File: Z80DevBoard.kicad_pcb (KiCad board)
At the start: 2 copper layers, 143 parts, among them SW1 WAIT, SW2 RESET, SW3 Z80BOOT, SW4 RPBOOT

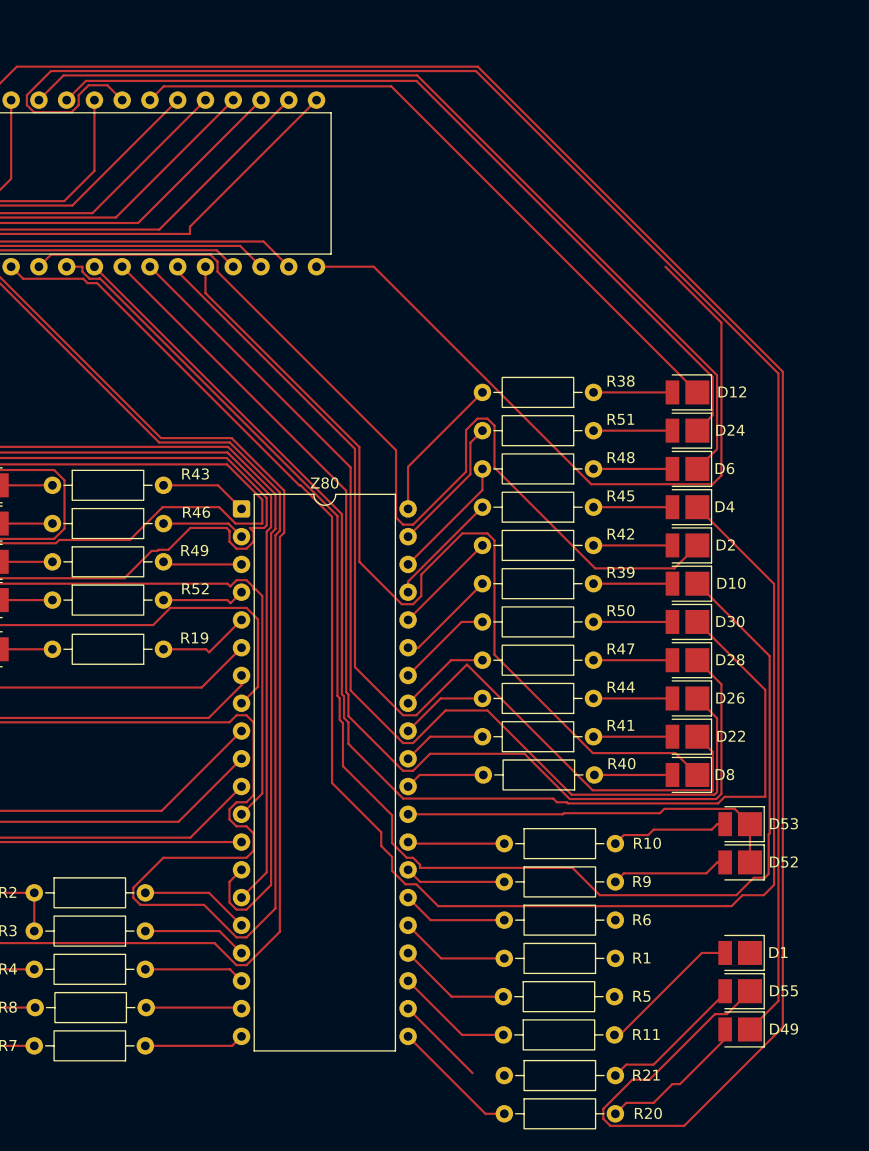
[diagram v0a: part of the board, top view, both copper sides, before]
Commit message: Fixed the GND of the Z80.
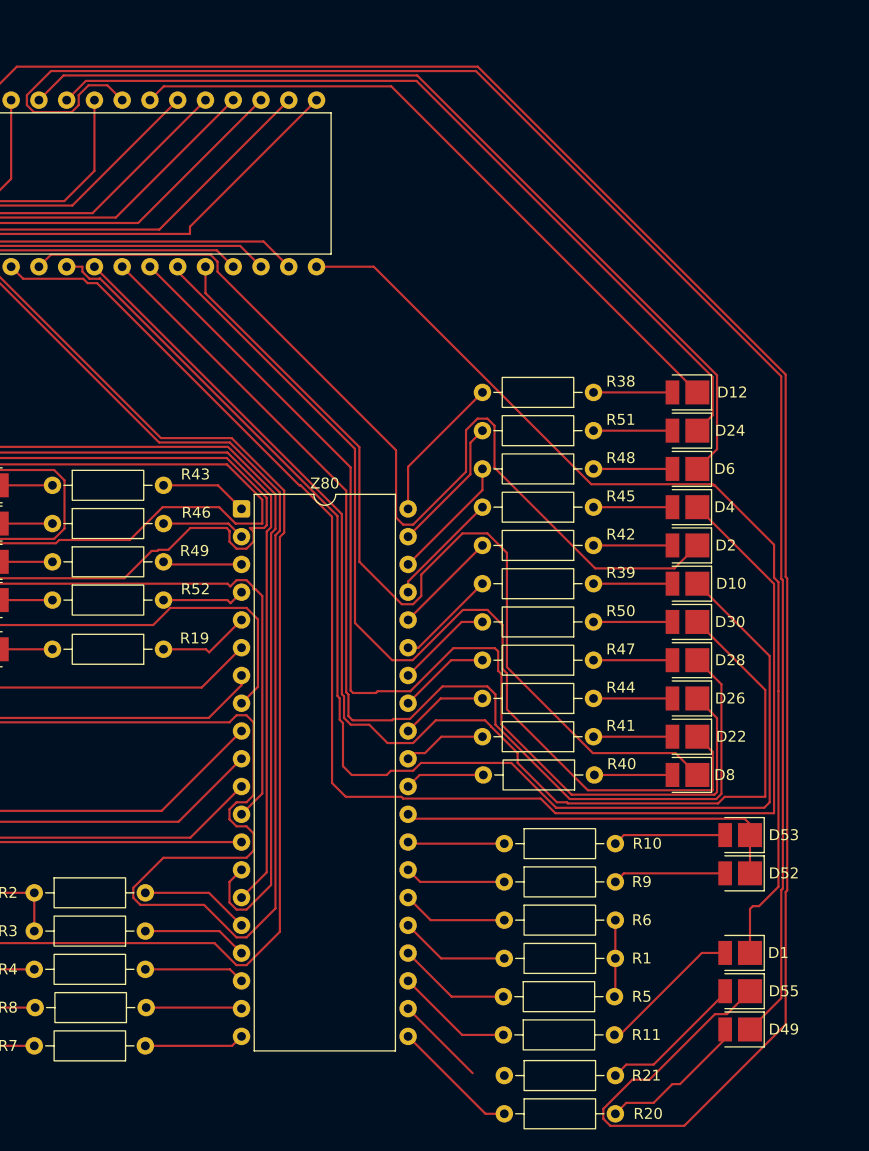
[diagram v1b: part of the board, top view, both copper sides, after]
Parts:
- moved D52 1.00 mm to (151.3, 159.0)
- moved D53 1.00 mm to (151.3, 155.5)
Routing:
- net GND: track 113.9 -> 139.0 mm
- net RAM-A7: track 148.1 -> 135.7 mm
- net RAM-A5: track 133.3 -> 122.1 mm
- net Vcc: track 77.8 -> 84.9 mm
- net RAM-A2: track 95.7 -> 100.4 mm
- net RAM-A3: track 101.6 -> 104.5 mm
- net RAM-A1: track 90.1 -> 92.0 mm
- net RAM-A4: track 112.5 -> 113.6 mm
- net Net-(D52-A): track 10.8 -> 11.6 mm

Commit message: Do things.
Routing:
- net GND: track 139.0 -> 230.5 mm
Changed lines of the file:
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@@
+	)
+	(segment
+		(start 104 176.5)
+		(end 103.5 177)
+		(width 0.2)
+		(layer "F.Cu")
+		(net 20)
+	)
+	(segment
+		(start 152.237 159)
+		(end 152.237 159.763)
+		(width 0.2)
+		(layer "F.Cu")
+		(net 20)
+	)
+	(segment
+		(start 127.8729 181.401)
+		(end 122.9719 176.5)
+		(width 0.2)
+		(layer "F.Cu")
+		(net 20)
+	)
+	(segment
+		(start 129.30395 182.101)
+		(end 128.659 181.45605)
+		(width 0.2)
+		(layer "F.Cu")
+		(net 20)
 	)
 	(segment
@@
 	)
 	(segment
+		(start 130.861 181.45605)
+		(end 130.21605 182.101)
+		(width 0.2)
+		(layer "F.Cu")
+		(net 20)
+	)
+	(segment
+		(start 152.237 159.763)
+		(end 130.861 181.139)
+		(width 0.2)
+		(layer "F.Cu")
+		(net 20)
+	)
+	(segment
 		(start 153.0671 162)
 		(end 152.5 162)
@@
 	)
 	(segment
+		(start 130.21605 182.101)
+		(end 129.30395 182.101)
+		(width 0.2)
+		(layer "F.Cu")
+		(net 20)
+	)
+	(segment
 		(start 152.237 162.263)
 		(end 152.237 166.283)
@@
 	)
 	(segment
+		(start 128.659 181.401)
+		(end 127.8729 181.401)
+		(width 0.2)
+		(layer "F.Cu")
+		(net 20)
+	)
+	(segment
 		(start 154.44 131.9529)
 		(end 154.841 132.3539)
@@
 	)
 	(segment
+		(start 122.9719 176.5)
+		(end 104 176.5)
+		(width 0.2)
+		(layer "F.Cu")
+		(net 20)
+	)
+	(segment
+		(start 130.861 181.139)
+		(end 130.861 181.45605)
+		(width 0.2)
+		(layer "F.Cu")
+		(net 20)
+	)
+	(segment
+		(start 128.659 181.45605)
+		(end 128.659 181.401)
+		(width 0.2)
+		(layer "F.Cu")
+		(net 20)
+	)
+	(segment
 		(start 91.95 20.6)
 		(end 91.95 21.8)
@@
 	)
 	(segment
+		(start 76.654 177)
+		(end 74.437 174.783)
+		(width 0.2)
+		(layer "F.Cu")
+		(net 20)
+	)
+	(segment
 		(start 98.55 20.6)
 		(end 98.05 20.6)
@@
 		(width 0.2)
 		(layer "F.Cu")
+		(net 20)
+	)
+	(segment
+		(start 103.5 177)
+		(end 76.654 177)
+		(width 0.2)
+		(layer "F.Cu")

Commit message: Do things.
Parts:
- moved RP2040_1 48.0 mm to (156.1, 73.2)
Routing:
- net CLOCK: track 75.3 -> 42.6 mm
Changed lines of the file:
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@@
 	(footprint "Package_DFN_QFN:QFN-56-1EP_7x7mm_P0.4mm_EP3.2x3.2mm"
 		(layer "F.Cu")
-		(at 109.68 60.895)
+		(at 156.0625 73.2)
 		(descr "QFN, 56 Pin (https://datasheets.raspberrypi.com/rp2040/rp2040-datasheet.pdf#page=607), generated with kicad-footprint-generator ipc_noLead_generator.py")
 		(tags "QFN NoLead")
@@
 	)
 	(segment
-		(start 105.717 138.358)
-		(end 102.075 142)
-		(width 0.2)
-		(layer "F.Cu")
-		(net 37)
-	)
-	(segment
 		(start 231.443 151.355)
 		(end 201.76795 151.355)
 		(width 0.2)
 		(layer "F.Cu")
-		(net 37)
-	)
-	(segment
-		(start 102.075 142)
-		(end 74.5 142)
-		(width 0.2)
-		(layer "F.Cu")

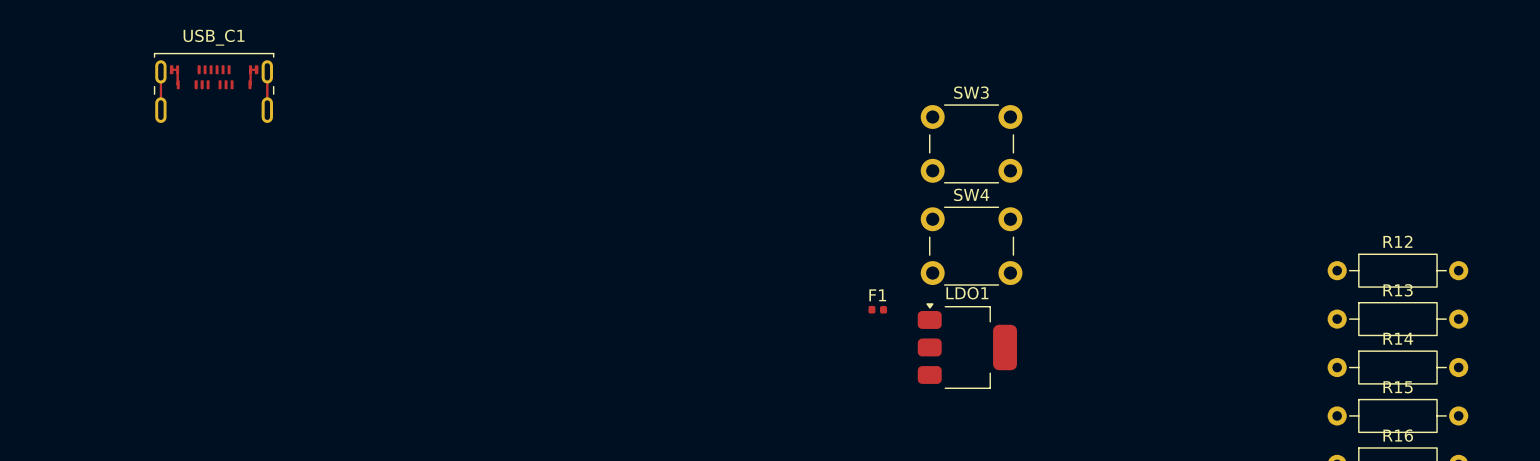
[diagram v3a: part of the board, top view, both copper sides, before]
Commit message: Added the second layer for the connections.
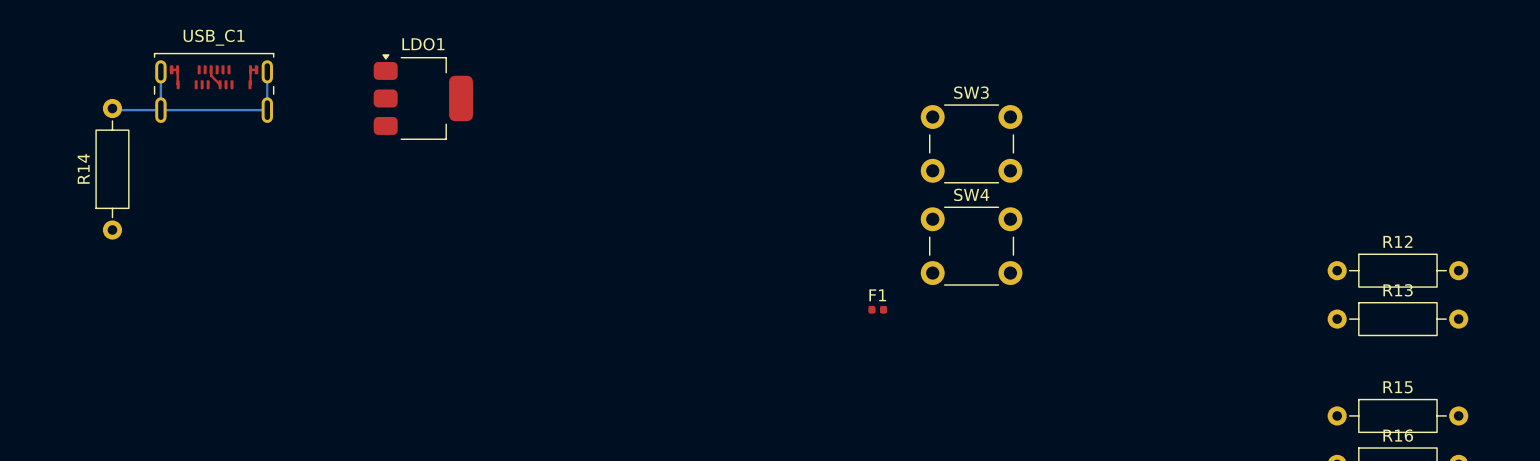
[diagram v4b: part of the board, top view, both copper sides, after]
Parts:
- moved R14 103.1 mm to (86.5, 34.0), turned to 90 degrees
- moved LDO1 50.0 mm to (112.5, 23.0)
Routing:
- net Net-(USB_C1-SHIELD): track 6.40 -> 19.4 mm
- net USB-RP2040-DP: track 0.00 -> 1.56 mm
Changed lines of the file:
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@@
 	(footprint "Package_TO_SOT_SMD:SOT-223-3_TabPin2"
 		(layer "F.Cu")
-		(at 157.995 43.825)
+		(at 112.5 23)
 		(descr "module CMS SOT223 4 pins")
 		(tags "CMS SOT")
@@
 	(footprint "Resistor_THT:R_Axial_DIN0207_L6.3mm_D2.5mm_P10.16mm_Horizontal"
 		(layer "F.Cu")
-		(at 188.92 45.5)
+		(at 86.5 34 90)
 		(descr "Resistor, Axial_DIN0207 series, Axial, Horizontal, pin pitch=10.16mm, 0.25W = 1/4W, length*diameter=6.3*2.5mm^2, http://cdn-reichelt.de/documents/datenblatt/B400/1_4W%23YAG.pdf")
 		(tags "Resistor Axial_DIN0207 series Axial Horizontal pin pitch 10.16mm 0.25W = 1/4W length 6.3mm diameter 2.5mm")
 		(property "Reference" "R14"
-			(at 5.08 -2.37 0)
+			(at 5.08 -2.37 90)
 			(layer "F.SilkS")
 			(effects
@@
 		)
 		(property "Value" "0"
-			(at 5.08 2.37 0)
+			(at 5.08 2.37 90)
 			(layer "F.Fab")
 			(effects
@@
 		)
 		(property "Datasheet" "~"
-			(at 0 0 0)
+			(at 0 0 90)
 			(layer "F.Fab")
 			(hide yes)
@@
 		)
 		(property "Description" "Resistor"
-			(at 0 0 0)
+			(at 0 0 90)
 			(layer "F.Fab")
 			(hide yes)
@@
 		(attr through_hole)
 		(fp_line
-			(start 1.04 0)
-			(end 1.81 0)
+			(start 9.12 0)
+			(end 8.35 0)
 			(stroke
 				(width 0.12)
@@
 		)
 		(fp_line
-			(start 9.12 0)
-			(end 8.35 0)
+			(start 1.04 0)
+			(end 1.81 0)
 			(stroke
 				(width 0.12)
@@
 		)
 		(fp_line
-			(start 0 0)
-			(end 1.93 0)
+			(start 10.16 0)
+			(end 8.23 0)
 			(stroke
 				(width 0.1)
@@
 		)
 		(fp_line
-			(start 10.16 0)
-			(end 8.23 0)
+			(start 0 0)
+			(end 1.93 0)
 			(stroke
 				(width 0.1)
@@
 		)
 		(fp_text user "${REFERENCE}"
-			(at 5.08 0 0)
+			(at 5.08 0 90)
 			(layer "F.Fab")
 			(effects
@@
 		)
 		(pad "1" thru_hole circle
-			(at 0 0)
+			(at 0 0 90)
 			(size 1.6 1.6)
 			(drill 0.8)
@@
 		)
 		(pad "2" thru_hole circle
-			(at 10.16 0)
+			(at 10.16 0 90)
 			(size 1.6 1.6)
 			(drill 0.8)
@@
 	)
 	(segment
-		(start 90.55 20.775)
+		(start 99.45 20.775)
+		(end 99.45 23.975)
+		(width 0.2)
+		(layer "B.Cu")
+		(net 171)
+	)
+	(segment
+		(start 90.55 23.975)
+		(end 90.55 20.775)
+		(width 0.2)
+		(layer "B.Cu")
+		(net 171)
+	)
+	(segment
+		(start 86.635 23.975)
+		(end 86.5 23.84)
+		(width 0.2)
+		(layer "B.Cu")
+		(net 171)
+	)
+	(segment
+		(start 99.45 23.975)
 		(end 90.55 23.975)
 		(width 0.2)
-		(layer "F.Cu")
+		(layer "B.Cu")
 		(net 171)
 	)
 	(segment
-		(start 99.45 20.775)
-		(end 99.45 23.975)
+		(start 90.55 23.975)
+		(end 86.635 23.975)
 		(width 0.2)
-		(layer "F.Cu")
+		(layer "B.Cu")
 		(net 171)
 	)
 	(segment
+		(start 94.75 20.6)
+		(end 94.75 21.1)
+		(width 0.2)
+		(layer "F.Cu")
+		(net 182)
+	)
+	(segment
+		(start 94.75 21.1)
+		(end 95.5 21.85)
+		(width 0.2)
+		(layer "F.Cu")
+		(net 182)
+	)
+	(segment

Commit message: Updated some connections from the first level connections to the second level connections.
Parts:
- moved SW1 89.8 mm to (219.7, 52.6)
- moved SW2 89.8 mm to (219.7, 42.6)
- moved LDO1 54.7 mm to (59.1, 35.2)
- moved R14 54.7 mm to (33.1, 46.2)
- moved USB_C1 54.7 mm to (41.6, 36.0)
- moved F1 51.2 mm to (201.4, 35.6)
- moved R12 51.2 mm to (239.8, 32.3)
- moved R13 51.2 mm to (239.8, 36.4)
- moved R15 51.2 mm to (239.8, 44.5)
- moved R16 51.2 mm to (239.8, 48.5)
- moved R17 51.2 mm to (239.8, 52.5)
- moved R18 51.2 mm to (239.8, 56.6)
- moved SW3 51.2 mm to (206.0, 19.4)
- moved SW4 51.2 mm to (206.0, 28.0)
- moved C1 51.2 mm to (274.9, 26.5)
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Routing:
- net RAM-Q0: track 80.8 -> 82.0 mm
- net RAM-Q7: track 148.6 -> 149.6 mm
- net RAM-Q2: track 106.0 -> 106.7 mm
- net RAM-Q1: track 94.0 -> 94.7 mm

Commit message: Started the connections with the RP2040. Started the vcc, gnd and 3v3 connections.
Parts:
- moved C8 214.6 mm to (60.5, 69.5)
- moved C1 212.8 mm to (66.5, 69.5)
- moved C2 206.0 mm to (72.5, 69.5)
- moved R13 202.2 mm to (38.9, 58.1), turned to -90 degrees
- moved R12 198.3 mm to (44.9, 68.3), turned to 90 degrees
- moved Flash1 145.0 mm to (211.9, 72.1)
- moved F1 136.3 mm to (66.3, 54.1), turned to 180 degrees
- moved C3 106.1 mm to (170.3, 54.0), turned to 90 degrees
- moved C4 100.6 mm to (175.2, 54.0), turned to 90 degrees
- moved C5 95.3 mm to (180.0, 54.0), turned to 90 degrees
- moved C6 90.1 mm to (184.8, 54.0), turned to 90 degrees
- moved R17 82.0 mm to (160.7, 74.0), turned to 180 degrees
- moved R18 80.1 mm to (160.6, 68.5), turned to 180 degrees
- moved C7 60.1 mm to (215.5, 65.0), turned to 90 degrees
- moved R15 46.8 mm to (202.4, 72.6), turned to 180 degrees
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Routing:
- net GND: track 230.5 -> 573.0 mm, vias 0 -> 3
- net Vdd_3v3: track 21.9 -> 358.2 mm, vias 0 -> 1
- net Vcc: track 84.9 -> 229.0 mm
- net RP2040-SH-GPIO3-SER: track 0.00 -> 123.8 mm
- net FLASH-DI-RP2040-QSPI_SD0: track 0.00 -> 49.2 mm, vias 0 -> 2
- net CLOCK: track 42.6 -> 0.45 mm
- net FLASH-CS-RP2040-QSPI_SS: track 0.00 -> 38.8 mm, vias 0 -> 2
- net FLASH-DO-RP2040-QSPI_SD1: track 0.00 -> 37.0 mm, vias 0 -> 2
- net USB-C-CC2: track 0.00 -> 31.5 mm
- net RP2040-SH-GPIO4-RCLK: track 0.00 -> 25.0 mm
- net RP2040-SH-GPIO2-SER: track 0.00 -> 23.2 mm
- net RP2040-RWRAM-GPIO8-PL: track 21.9 -> 0.00 mm
- net RP2040-DVDD: track 0.00 -> 18.6 mm
- net RP2040-VREG_VOUT: track 0.00 -> 17.1 mm
- net USB-C-CC1: track 0.00 -> 15.9 mm
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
